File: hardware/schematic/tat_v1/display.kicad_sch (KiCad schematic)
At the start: 17 parts, among them J4 24-pin FPC 0.5mm, Top Contact, Q1 Q_NMOS

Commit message: Added new titles to sheets
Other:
- title: (none) -> Tiny Ambient Tracker - Eink display
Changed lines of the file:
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@@
 	(generator_version "9.0")
 	(paper "A4")
+	(title_block
+		(title "Tiny Ambient Tracker - Eink display")
+	)
 	(text "Display Driver circuit"
 		(exclude_from_sim no)

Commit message: Used auto reference designator on whole schematic
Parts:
- renumbered C20 to C24, C21 to C25, C22 to C26, C23 to C27, C29 to C28, C25 to C29, C26 to C30, C27 to C31, C28 to C32, D5 to D4, D6 to D5, D7 to D6, R24 to R28, R23 to R29
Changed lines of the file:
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@@
 		(dnp no)
 		(fields_autoplaced yes)
-		(property "Reference" "#PWR050"
+		(property "Reference" "#PWR052"
 			(at 68.58 134.62 0)
 			(effects
@@
 			(project "tat_v1"
 				(path "/b6d2ddf1-6792-45dd-afc9-29fd74d587ec/3e709284-5543-4534-bf58-110f53ad5a3b"
-					(reference "#PWR050")
+					(reference "#PWR052")
 					(unit 1)
 				)
@@
 		(on_board yes)
 		(dnp no)
-		(property "Reference" "D7"
+		(property "Reference" "D6"
 			(at 87.63 101.6 0)
 			(effects
@@
 			(project "tat_v1"
 				(path "/b6d2ddf1-6792-45dd-afc9-29fd74d587ec/3e709284-5543-4534-bf58-110f53ad5a3b"
-					(reference "D7")
+					(reference "D6")
 					(unit 1)
 				)
@@
 		(on_board yes)
 		(dnp no)
-		(property "Reference" "C28"
+		(property "Reference" "C32"
 			(at 231.648 123.952 90)
 			(effects
@@
 			(project "tat_v1"
 				(path "/b6d2ddf1-6792-45dd-afc9-29fd74d587ec/3e709284-5543-4534-bf58-110f53ad5a3b"
-					(reference "C28")
+					(reference "C32")
 					(unit 1)
 				)
@@
 		(on_board yes)
 		(dnp no)
-		(property "Reference" "C27"
+		(property "Reference" "C31"
 			(at 231.648 110.236 90)
 			(effects
@@
 			(project "tat_v1"
 				(path "/b6d2ddf1-6792-45dd-afc9-29fd74d587ec/3e709284-5543-4534-bf58-110f53ad5a3b"
-					(reference "C27")
+					(reference "C31")
 					(unit 1)
 				)
@@
 		(on_board yes)
 		(dnp no)
-		(property "Reference" "C20"
+		(property "Reference" "C24"
 			(at 36.83 104.14 0)
 			(effects
@@
 			(project "tat_v1"
 				(path "/b6d2ddf1-6792-45dd-afc9-29fd74d587ec/3e709284-5543-4534-bf58-110f53ad5a3b"
-					(reference "C20")
+					(reference "C24")
 					(unit 1)
 				)
@@
 		(on_board yes)
 		(dnp no)
-		(property "Reference" "C25"
+		(property "Reference" "C29"
 			(at 231.648 87.376 90)
 			(effects
@@
 			(project "tat_v1"
 				(path "/b6d2ddf1-6792-45dd-afc9-29fd74d587ec/3e709284-5543-4534-bf58-110f53ad5a3b"
-					(reference "C25")
+					(reference "C29")
 					(unit 1)
 				)
@@
 		(on_board yes)
 		(dnp no)
-		(property "Reference" "C23"
+		(property "Reference" "C27"
 			(at 136.652 122.936 90)
 			(effects
@@
 			(project "tat_v1"
 				(path "/b6d2ddf1-6792-45dd-afc9-29fd74d587ec/3e709284-5543-4534-bf58-110f53ad5a3b"
-					(reference "C23")
+					(reference "C27")
 					(unit 1)
 				)
@@
 		(on_board yes)
 		(dnp no)
-		(property "Reference" "R24"
+		(property "Reference" "R28"
 			(at 59.944 119.38 0)
 			(effects
@@
 			(project "tat_v1"
 				(path "/b6d2ddf1-6792-45dd-afc9-29fd74d587ec/3e709284-5543-4534-bf58-110f53ad5a3b"
-					(reference "R24")
+					(reference "R28")
 					(unit 1)
 				)
@@
 		(dnp no)
 		(fields_autoplaced yes)
-		(property "Reference" "#PWR053"
+		(property "Reference" "#PWR055"
 			(at 129.54 127 0)
 			(effects
@@
 			(project "tat_v1"
 				(path "/b6d2ddf1-6792-45dd-afc9-29fd74d587ec/3e709284-5543-4534-bf58-110f53ad5a3b"
-					(reference "#PWR053")
+					(reference "#PWR055")
 					(unit 1)
 				)
@@
 		(dnp no)
 		(fields_autoplaced yes)
-		(property "Reference" "#PWR051"
+		(property "Reference" "#PWR053"
 			(at 93.98 88.9 0)
 			(effects
@@
 			(project "tat_v1"
 				(path "/b6d2ddf1-6792-45dd-afc9-29fd74d587ec/3e709284-5543-4534-bf58-110f53ad5a3b"
-					(reference "#PWR051")
+					(reference "#PWR053")
 					(unit 1)
 				)
@@
 		(on_board yes)
 		(dnp no)
-		(property "Reference" "#PWR048"
+		(property "Reference" "#PWR050"
 			(at 36.83 101.6 0)
 			(effects
@@
 			(project ""
 				(path "/b6d2ddf1-6792-45dd-afc9-29fd74d587ec/3e709284-5543-4534-bf58-110f53ad5a3b"
-					(reference "#PWR048")
+					(reference "#PWR050")
 					(unit 1)
 				)
@@
 		(on_board yes)
 		(dnp no)
-		(property "Reference" "C22"
+		(property "Reference" "C26"
 			(at 102.87 104.14 0)
 			(effects
@@
 			(project "tat_v1"
 				(path "/b6d2ddf1-6792-45dd-afc9-29fd74d587ec/3e709284-5543-4534-bf58-110f53ad5a3b"
-					(reference "C22")
+					(reference "C26")
 					(unit 1)
 				)
@@
 		(dnp no)
 		(fields_autoplaced yes)
-		(property "Reference" "#PWR049"
+		(property "Reference" "#PWR051"
 			(at 43.18 118.11 0)
 			(effects
@@
 			(project ""
 				(path "/b6d2ddf1-6792-45dd-afc9-29fd74d587ec/3e709284-5543-4534-bf58-110f53ad5a3b"
-					(reference "#PWR049")
+					(reference "#PWR051")
 					(unit 1)
 				)
@@
 		(on_board yes)
 		(dnp no)
-		(property "Reference" "D6"
+		(property "Reference" "D5"
 			(at 83.82 83.82 0)
 			(effects
@@
 			(project "tat_v1"
 				(path "/b6d2ddf1-6792-45dd-afc9-29fd74d587ec/3e709284-5543-4534-bf58-110f53ad5a3b"
-					(reference "D6")
+					(reference "D5")
 					(unit 1)
 				)
@@
 		(on_board yes)
 		(dnp no)
-		(property "Reference" "R23"
+		(property "Reference" "R29"
 			(at 70.104 119.38 0)
 			(effects
@@
 			(project ""
 				(path "/b6d2ddf1-6792-45dd-afc9-29fd74d587ec/3e709284-5543-4534-bf58-110f53ad5a3b"
-					(reference "R23")
+					(reference "R29")
 					(unit 1)
 				)
@@
 		(dnp no)
 		(fields_autoplaced yes)
-		(property "Reference" "#PWR052"
+		(property "Reference" "#PWR054"
 			(at 100.33 118.11 0)
 			(effects
@@
 			(project "tat_v1"
 				(path "/b6d2ddf1-6792-45dd-afc9-29fd74d587ec/3e709284-5543-4534-bf58-110f53ad5a3b"
-					(reference "#PWR052")
+					(reference "#PWR054")
 					(unit 1)
 				)
@@
 		(on_board yes)
 		(dnp no)
-		(property "Reference" "D5"
+		(property "Reference" "D4"
 			(at 83.82 68.58 0)
 			(effects
@@
 			(project ""
 				(path "/b6d2ddf1-6792-45dd-afc9-29fd74d587ec/3e709284-5543-4534-bf58-110f53ad5a3b"
-					(reference "D5")
+					(reference "D4")
 					(unit 1)
 				)
@@
 		(on_board yes)
 		(dnp no)
-		(property "Reference" "C29"
+		(property "Reference" "C28"
 			(at 203.962 84.074 0)
 			(effects
@@
 			(project "tat_v1"
 				(path "/b6d2ddf1-6792-45dd-afc9-29fd74d587ec/3e709284-5543-4534-bf58-110f53ad5a3b"
-					(reference "C29")
+					(reference "C28")
 					(unit 1)
 				)
@@
 		(on_board yes)
 		(dnp no)
-		(property "Reference" "C21"
+		(property "Reference" "C25"
 			(at 71.12 91.44 0)
 			(effects
@@
 			(project "tat_v1"
 				(path "/b6d2ddf1-6792-45dd-afc9-29fd74d587ec/3e709284-5543-4534-bf58-110f53ad5a3b"
-					(reference "C21")
+					(reference "C25")
 					(unit 1)
 				)
@@
 		(on_board yes)
 		(dnp no)
-		(property "Reference" "#PWR054"
+		(property "Reference" "#PWR056"
 			(at 209.55 76.2 0)
 			(effects
@@
 			(project "tat_v1"
 				(path "/b6d2ddf1-6792-45dd-afc9-29fd74d587ec/3e709284-5543-4534-bf58-110f53ad5a3b"
-					(reference "#PWR054")
+					(reference "#PWR056")
 					(unit 1)
 				)
@@
 		(dnp no)
 		(fields_autoplaced yes)
-		(property "Reference" "#PWR055"
+		(property "Reference" "#PWR057"
 			(at 222.25 135.89 0)
 			(effects
@@
 			(project "tat_v1"
 				(path "/b6d2ddf1-6792-45dd-afc9-29fd74d587ec/3e709284-5543-4534-bf58-110f53ad5a3b"
-					(reference "#PWR055")
+					(reference "#PWR057")
 					(unit 1)
 				)
@@
 		(on_board yes)
 		(dnp no)
-		(property "Reference" "C26"
+		(property "Reference" "C30"
 			(at 231.648 96.266 90)
 			(effects
@@
 			(project "tat_v1"
 				(path "/b6d2ddf1-6792-45dd-afc9-29fd74d587ec/3e709284-5543-4534-bf58-110f53ad5a3b"
-					(reference "C26")
-					(unit 1)
-				)
+					(reference "C30")
+					(unit 1)
+				)

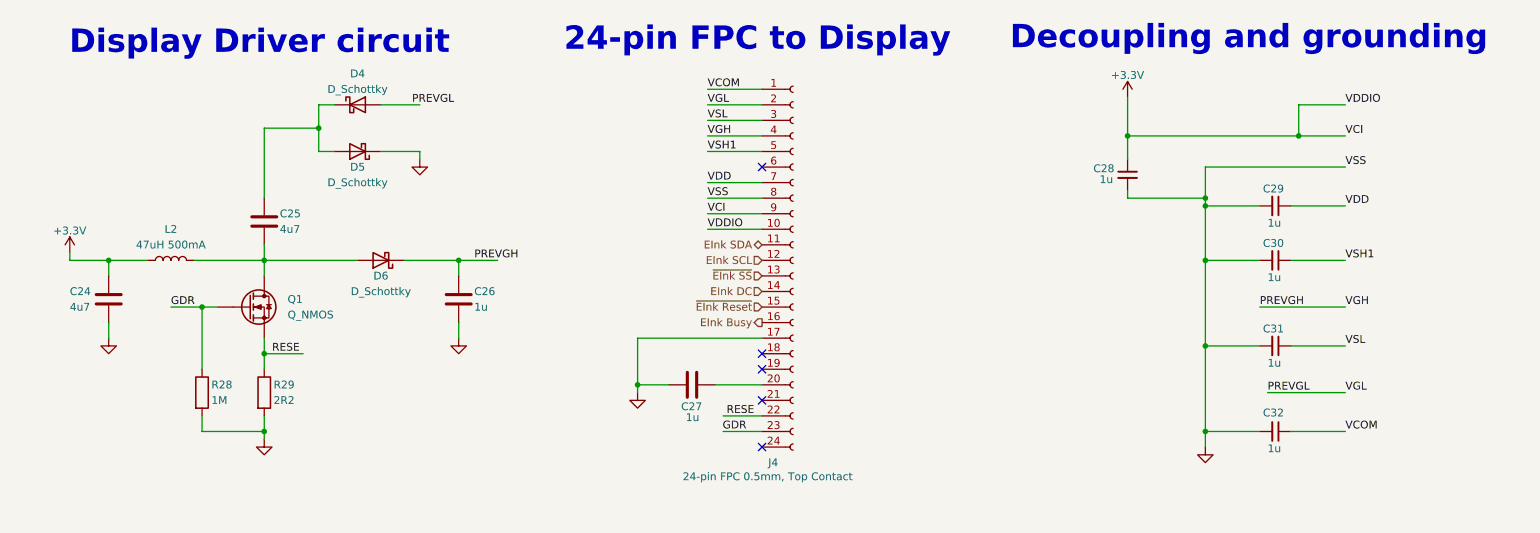
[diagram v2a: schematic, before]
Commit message: Fixed all ERC errors and warnings
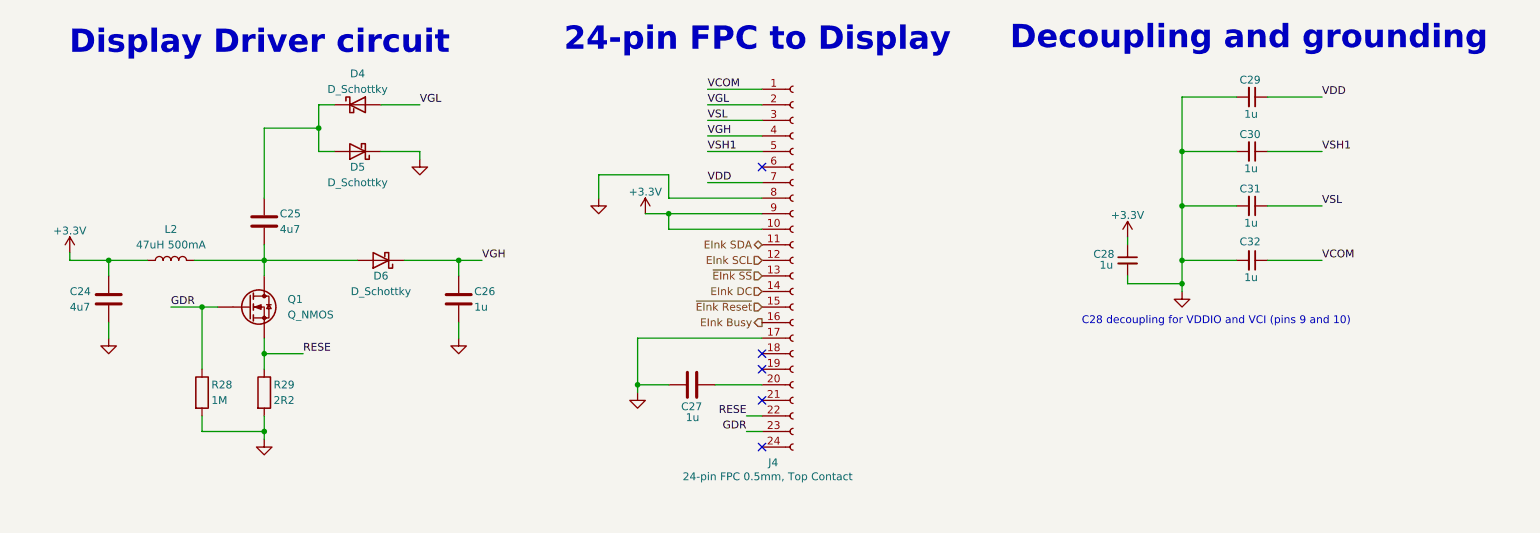
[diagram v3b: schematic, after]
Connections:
- net PREVGH renamed VGH
- net PREVGL renamed VGL
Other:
- note added: "C28 decoupling for VDDIO and VCI (pins 9 and 10)"
- moved on the sheet: C28, C29, C30, C31, C32

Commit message: Continuing with setting basic footprints for parts
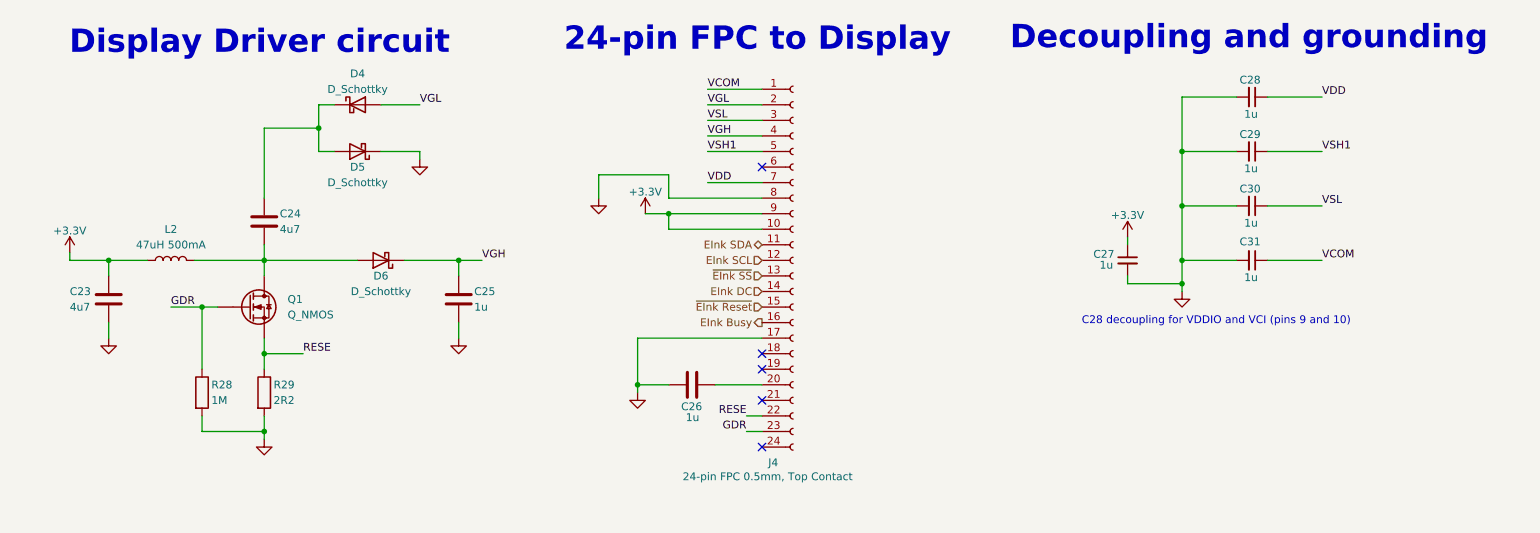
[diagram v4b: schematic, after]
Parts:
- renumbered C24 to C23, C25 to C24, C26 to C25, C27 to C26, C28 to C27, C29 to C28, C30 to C29, C31 to C30, C32 to C31
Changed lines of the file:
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@@
 		(dnp no)
 		(fields_autoplaced yes)
-		(property "Reference" "#PWR052"
+		(property "Reference" "#PWR051"
 			(at 68.58 134.62 0)
 			(effects
@@
 			(project "tat_v1"
 				(path "/b6d2ddf1-6792-45dd-afc9-29fd74d587ec/3e709284-5543-4534-bf58-110f53ad5a3b"
-					(reference "#PWR052")
+					(reference "#PWR051")
 					(unit 1)
 				)
@@
 		(on_board yes)
 		(dnp no)
-		(property "Reference" "C32"
+		(property "Reference" "C31"
 			(at 227.838 96.012 90)
 			(effects
@@
 			(project "tat_v1"
 				(path "/b6d2ddf1-6792-45dd-afc9-29fd74d587ec/3e709284-5543-4534-bf58-110f53ad5a3b"
-					(reference "C32")
+					(reference "C31")
 					(unit 1)
 				)
@@
 		(on_board yes)
 		(dnp no)
-		(property "Reference" "C31"
+		(property "Reference" "C30"
 			(at 227.838 87.376 90)
 			(effects
@@
 			(project "tat_v1"
 				(path "/b6d2ddf1-6792-45dd-afc9-29fd74d587ec/3e709284-5543-4534-bf58-110f53ad5a3b"
-					(reference "C31")
+					(reference "C30")
 					(unit 1)
 				)
@@
 		(dnp no)
 		(fields_autoplaced yes)
-		(property "Reference" "#PWR055"
+		(property "Reference" "#PWR054"
 			(at 123.19 95.25 0)
 			(effects
@@
 			(project "tat_v1"
 				(path "/b6d2ddf1-6792-45dd-afc9-29fd74d587ec/3e709284-5543-4534-bf58-110f53ad5a3b"
-					(reference "#PWR055")
+					(reference "#PWR054")
 					(unit 1)
 				)
@@
 		(on_board yes)
 		(dnp no)
-		(property "Reference" "C24"
+		(property "Reference" "C23"
 			(at 36.83 104.14 0)
 			(effects
@@
 			(project "tat_v1"
 				(path "/b6d2ddf1-6792-45dd-afc9-29fd74d587ec/3e709284-5543-4534-bf58-110f53ad5a3b"
-					(reference "C24")
+					(reference "C23")
 					(unit 1)
 				)
@@
 		(on_board yes)
 		(dnp no)
-		(property "Reference" "C29"
+		(property "Reference" "C28"
 			(at 227.838 69.596 90)
 			(effects
@@
 			(project "tat_v1"
 				(path "/b6d2ddf1-6792-45dd-afc9-29fd74d587ec/3e709284-5543-4534-bf58-110f53ad5a3b"
-					(reference "C29")
+					(reference "C28")
 					(unit 1)
 				)
@@
 		(on_board yes)
 		(dnp no)
-		(property "Reference" "C27"
+		(property "Reference" "C26"
 			(at 136.652 122.936 90)
 			(effects
@@
 			(project "tat_v1"
 				(path "/b6d2ddf1-6792-45dd-afc9-29fd74d587ec/3e709284-5543-4534-bf58-110f53ad5a3b"
-					(reference "C27")
+					(reference "C26")
 					(unit 1)
 				)
@@
 		(dnp no)
 		(fields_autoplaced yes)
-		(property "Reference" "#PWR056"
+		(property "Reference" "#PWR055"
 			(at 129.54 127 0)
 			(effects
@@
 			(project "tat_v1"
 				(path "/b6d2ddf1-6792-45dd-afc9-29fd74d587ec/3e709284-5543-4534-bf58-110f53ad5a3b"
-					(reference "#PWR056")
+					(reference "#PWR055")
 					(unit 1)
 				)
@@
 		(dnp no)
 		(fields_autoplaced yes)
-		(property "Reference" "#PWR053"
+		(property "Reference" "#PWR052"
 			(at 93.98 88.9 0)
 			(effects
@@
 			(project "tat_v1"
 				(path "/b6d2ddf1-6792-45dd-afc9-29fd74d587ec/3e709284-5543-4534-bf58-110f53ad5a3b"
-					(reference "#PWR053")
+					(reference "#PWR052")
 					(unit 1)
 				)
@@
 		(on_board yes)
 		(dnp no)
-		(property "Reference" "#PWR050"
+		(property "Reference" "#PWR049"
 			(at 36.83 101.6 0)
 			(effects
@@
 			(project ""
 				(path "/b6d2ddf1-6792-45dd-afc9-29fd74d587ec/3e709284-5543-4534-bf58-110f53ad5a3b"
-					(reference "#PWR050")
+					(reference "#PWR049")
 					(unit 1)
 				)
@@
 		(on_board yes)
 		(dnp no)
-		(property "Reference" "C26"
+		(property "Reference" "C25"
 			(at 102.87 104.14 0)
 			(effects
@@
 			(project "tat_v1"
 				(path "/b6d2ddf1-6792-45dd-afc9-29fd74d587ec/3e709284-5543-4534-bf58-110f53ad5a3b"
-					(reference "C26")
+					(reference "C25")
 					(unit 1)
 				)
@@
 		(dnp no)
 		(fields_autoplaced yes)
-		(property "Reference" "#PWR051"
+		(property "Reference" "#PWR050"
 			(at 43.18 118.11 0)
 			(effects
@@
 			(project ""
 				(path "/b6d2ddf1-6792-45dd-afc9-29fd74d587ec/3e709284-5543-4534-bf58-110f53ad5a3b"
-					(reference "#PWR051")
+					(reference "#PWR050")
 					(unit 1)
 				)
@@
 		(on_board yes)
 		(dnp no)
-		(property "Reference" "#PWR057"
+		(property "Reference" "#PWR056"
 			(at 130.81 95.25 0)
 			(effects
@@
 			(project "tat_v1"
 				(path "/b6d2ddf1-6792-45dd-afc9-29fd74d587ec/3e709284-5543-4534-bf58-110f53ad5a3b"
-					(reference "#PWR057")
+					(reference "#PWR056")
 					(unit 1)
 				)
@@
 		(dnp no)
 		(fields_autoplaced yes)
-		(property "Reference" "#PWR054"
+		(property "Reference" "#PWR053"
 			(at 100.33 118.11 0)
 			(effects
@@
 			(project "tat_v1"
 				(path "/b6d2ddf1-6792-45dd-afc9-29fd74d587ec/3e709284-5543-4534-bf58-110f53ad5a3b"
-					(reference "#PWR054")
+					(reference "#PWR053")
 					(unit 1)
 				)
@@
 		(on_board yes)
 		(dnp no)
-		(property "Reference" "C28"
+		(property "Reference" "C27"
 			(at 203.962 98.044 0)
 			(effects
@@
 			(project "tat_v1"
 				(path "/b6d2ddf1-6792-45dd-afc9-29fd74d587ec/3e709284-5543-4534-bf58-110f53ad5a3b"
-					(reference "C28")
+					(reference "C27")
 					(unit 1)
 				)
@@
 		(on_board yes)
 		(dnp no)
-		(property "Reference" "C25"
+		(property "Reference" "C24"
 			(at 71.12 91.44 0)
 			(effects
@@
 			(project "tat_v1"
 				(path "/b6d2ddf1-6792-45dd-afc9-29fd74d587ec/3e709284-5543-4534-bf58-110f53ad5a3b"
-					(reference "C25")
+					(reference "C24")
 					(unit 1)
 				)
@@
 		(on_board yes)
 		(dnp no)
-		(property "Reference" "#PWR058"
+		(property "Reference" "#PWR057"
 			(at 209.55 99.06 0)
 			(effects
@@
 			(project "tat_v1"
 				(path "/b6d2ddf1-6792-45dd-afc9-29fd74d587ec/3e709284-5543-4534-bf58-110f53ad5a3b"
-					(reference "#PWR058")
+					(reference "#PWR057")
 					(unit 1)
 				)
@@
 		(dnp no)
 		(fields_autoplaced yes)
-		(property "Reference" "#PWR059"
+		(property "Reference" "#PWR058"
 			(at 218.44 110.49 0)
 			(effects
@@
 			(project "tat_v1"
 				(path "/b6d2ddf1-6792-45dd-afc9-29fd74d587ec/3e709284-5543-4534-bf58-110f53ad5a3b"
-					(reference "#PWR059")
+					(reference "#PWR058")
 					(unit 1)
 				)
@@
 		(on_board yes)
 		(dnp no)
-		(property "Reference" "C30"
+		(property "Reference" "C29"
 			(at 227.838 78.486 90)
 			(effects
@@
 			(project "tat_v1"
 				(path "/b6d2ddf1-6792-45dd-afc9-29fd74d587ec/3e709284-5543-4534-bf58-110f53ad5a3b"
-					(reference "C30")
-					(unit 1)
-				)
+					(reference "C29")
+					(unit 1)
+				)
